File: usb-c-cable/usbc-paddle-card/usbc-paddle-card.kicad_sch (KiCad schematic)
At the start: 7 parts, among them J1 USB_C_Receptacle, P1 PAD_SMD, P2 PAD_SMD, P3 PAD_SMD, P4 PAD_SMD, P5 PAD_SMD

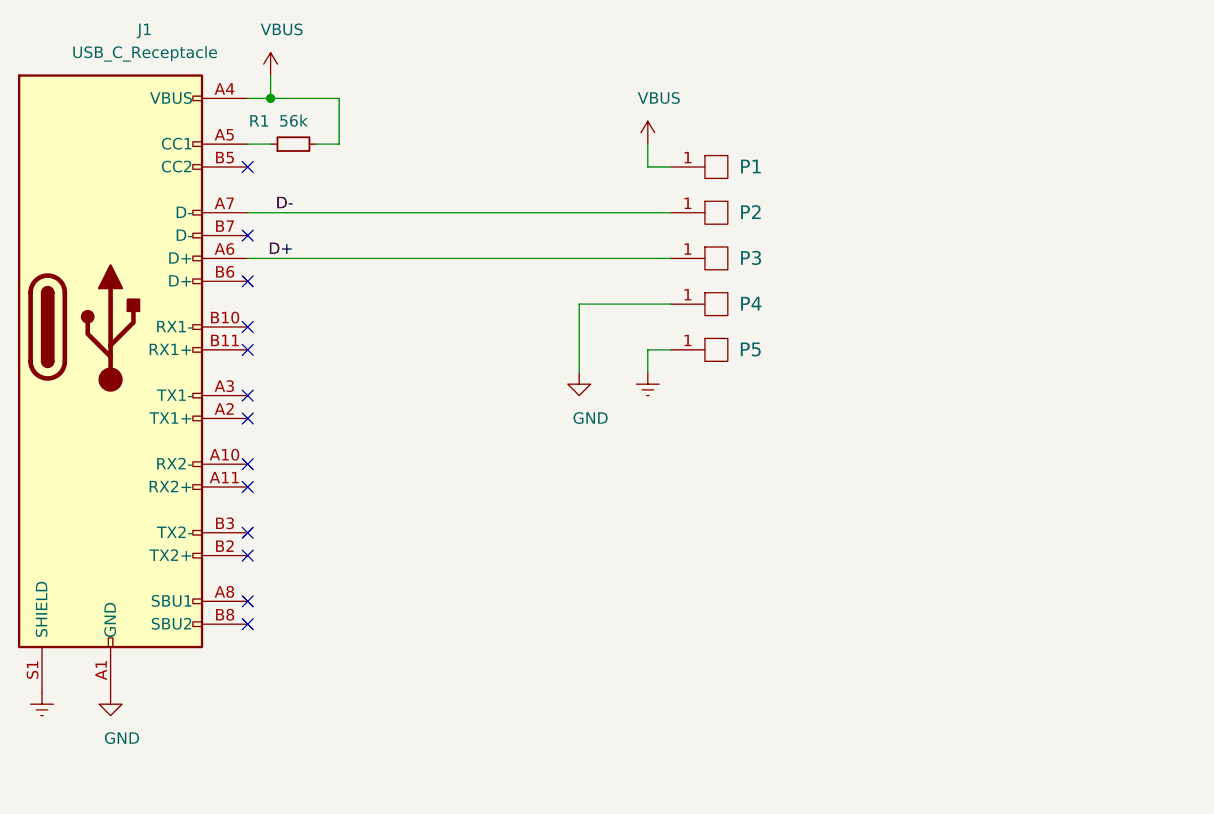
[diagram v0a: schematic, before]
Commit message: Added resistor value for up-stream facing paddle use.
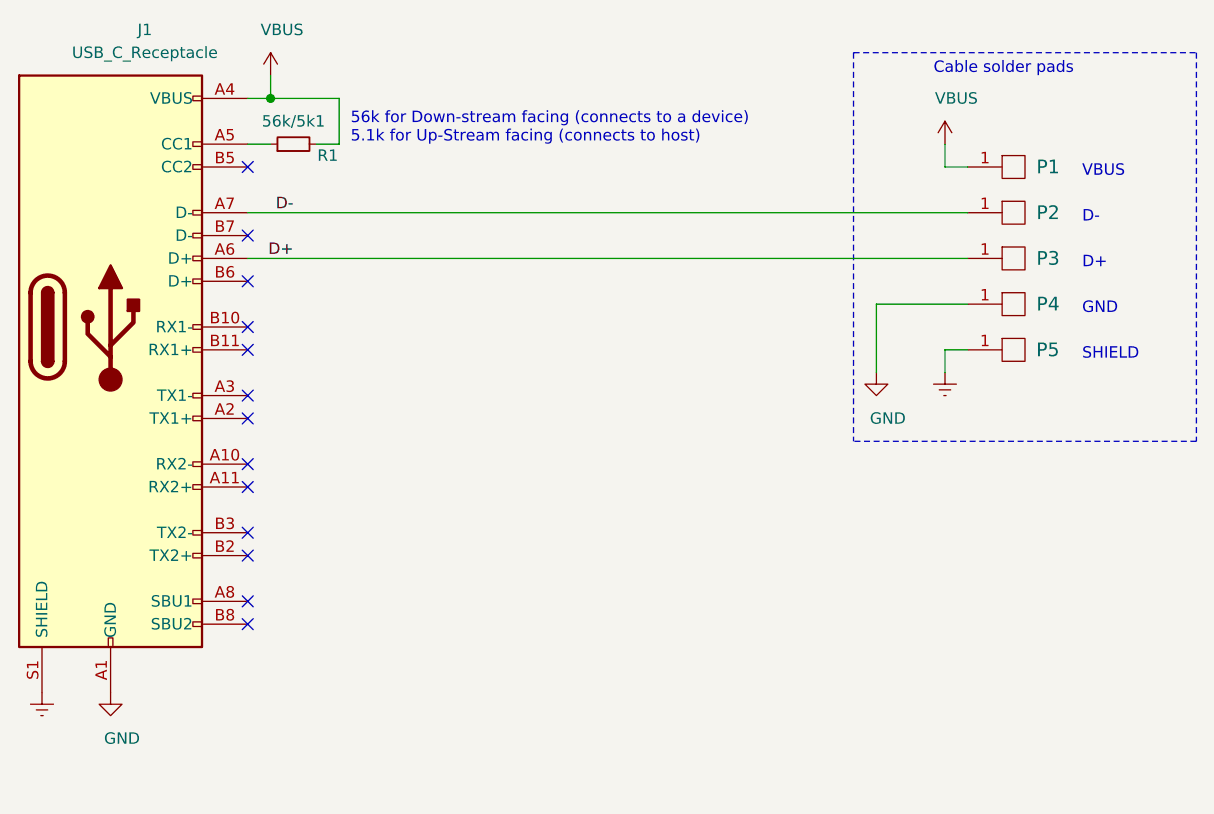
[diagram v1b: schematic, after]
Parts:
- R1: value 56k -> 56k/5k1
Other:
- note added: "56k for Down-stream facing (connects to a device) 5.1k for Up-Stream facing (connects to host)"
- note added: "Cable solder pads"
- note added: "D+"
- note added: "D-"
- note added: "GND"
- note added: "SHIELD"
- note added: "VBUS"
- moved on the sheet: P1, P2, P3, P4, P5

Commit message: Added resistor for Up-Stream use.
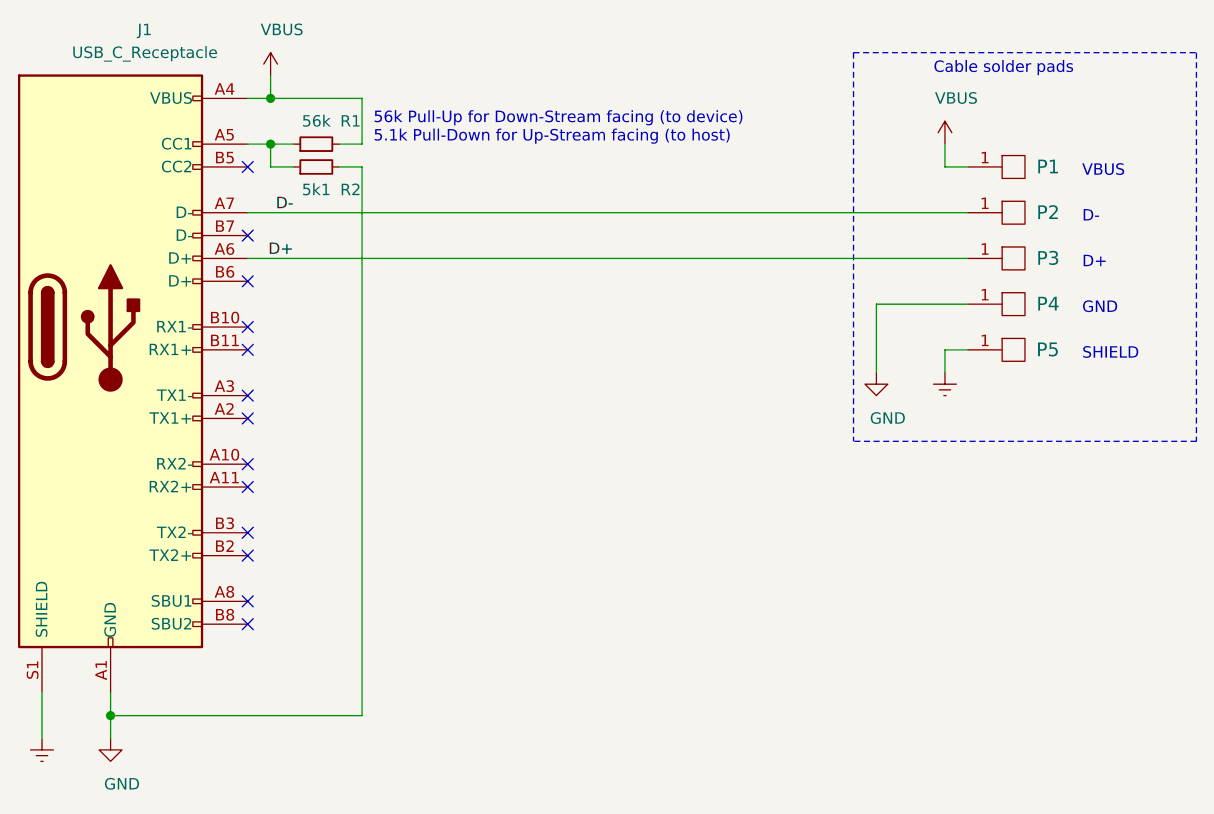
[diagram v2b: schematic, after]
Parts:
- added R2: 5k1, pkl_dipol:R_0402, symbol pkl_device:pkl_R_Small
- R1: value 56k/5k1 -> 56k
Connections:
- net GND: now also R2.2
- net at J1.A5 (CC1), R1.1: now also R2.1
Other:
- note added: "56k Pull-Up for Down-Stream facing (to device) 5.1k Pull-Down for Up-Stream facing (to host)"
- note removed: "56k for Down-stream facing (connects to a device) 5.1k for Up-Stream facing (connects to host)"
- moved on the sheet: R1
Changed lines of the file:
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@@
   (page 1 1)
   (paper "A4")
+  (junction (at 36.83 107.95) (diameter 1.016) (color 0 0 0 0))
   (junction (at 54.61 39.37) (diameter 1.016) (color 0 0 0 0))
+  (junction (at 54.61 44.45) (diameter 1.016) (color 0 0 0 0))
+  (no_connect (at 52.07 74.93))
+  (no_connect (at 52.07 90.17))
+  (no_connect (at 52.07 46.99))
+  (no_connect (at 52.07 95.25))
+  (no_connect (at 52.07 80.01))
+  (no_connect (at 52.07 54.61))
+  (no_connect (at 52.07 59.69))
   (no_connect (at 52.07 64.77))
+  (no_connect (at 52.07 72.39))
   (no_connect (at 52.07 67.31))
-  (no_connect (at 52.07 46.99))
   (no_connect (at 52.07 97.79))
-  (no_connect (at 52.07 72.39))
-  (no_connect (at 52.07 95.25))
-  (no_connect (at 52.07 90.17))
-  (no_connect (at 52.07 54.61))
+  (no_connect (at 52.07 82.55))
   (no_connect (at 52.07 87.63))
-  (no_connect (at 52.07 74.93))
-  (no_connect (at 52.07 80.01))
-  (no_connect (at 52.07 59.69))
-  (no_connect (at 52.07 82.55))
+  (wire (pts (xy 29.21 110.49) (xy 29.21 105.41))
+    (stroke (width 0) (type solid) (color 0 0 0 0))
+  )
+  (wire (pts (xy 36.83 107.95) (xy 36.83 105.41))
+    (stroke (width 0) (type solid) (color 0 0 0 0))
+  )
+  (wire (pts (xy 36.83 107.95) (xy 64.77 107.95))
+    (stroke (width 0) (type solid) (color 0 0 0 0))
+  )
+  (wire (pts (xy 36.83 110.49) (xy 36.83 107.95))
+    (stroke (width 0) (type solid) (color 0 0 0 0))
+  )
   (wire (pts (xy 52.07 39.37) (xy 54.61 39.37))
     (stroke (width 0) (type solid) (color 0 0 0 0))
@@
     (stroke (width 0) (type solid) (color 0 0 0 0))
   )
-  (wire (pts (xy 54.61 39.37) (xy 62.23 39.37))
-    (stroke (width 0) (type solid) (color 0 0 0 0))
-  )
-  (wire (pts (xy 59.69 44.45) (xy 62.23 44.45))
-    (stroke (width 0) (type solid) (color 0 0 0 0))
-  )
-  (wire (pts (xy 62.23 44.45) (xy 62.23 39.37))
+  (wire (pts (xy 54.61 39.37) (xy 64.77 39.37))
+    (stroke (width 0) (type solid) (color 0 0 0 0))
+  )
+  (wire (pts (xy 54.61 44.45) (xy 57.15 44.45))
+    (stroke (width 0) (type solid) (color 0 0 0 0))
+  )
+  (wire (pts (xy 54.61 46.99) (xy 54.61 44.45))
+    (stroke (width 0) (type solid) (color 0 0 0 0))
+  )
+  (wire (pts (xy 57.15 46.99) (xy 54.61 46.99))
+    (stroke (width 0) (type solid) (color 0 0 0 0))
+  )
+  (wire (pts (xy 62.23 44.45) (xy 64.77 44.45))
+    (stroke (width 0) (type solid) (color 0 0 0 0))
+  )
+  (wire (pts (xy 64.77 44.45) (xy 64.77 39.37))
+    (stroke (width 0) (type solid) (color 0 0 0 0))
+  )
+  (wire (pts (xy 64.77 46.99) (xy 62.23 46.99))
+    (stroke (width 0) (type solid) (color 0 0 0 0))
+  )
+  (wire (pts (xy 64.77 107.95) (xy 64.77 46.99))
     (stroke (width 0) (type solid) (color 0 0 0 0))
   )
@@
     (stroke (width 0) (type dash) (color 0 0 0 0))
   )
-  (text "56k for Down-stream facing (connects to a device)\n5.1k for Up-Stream facing (connects to host)"
-    (at 63.5 44.45 0)
+  (text "56k Pull-Up for Down-Stream facing (to device)\n5.1k Pull-Down for Up-Stream facing (to host)"
+    (at 66.04 44.45 0)
     (effects (font (size 1.27 1.27)) (justify left bottom))
   )
@@
     )
   )
-  (symbol (lib_id "power:Earth") (at 29.21 105.41 0) (unit 1)
-    (in_bom yes) (on_board yes)
-    (property "Reference" "#PWR0101" (id 0) (at 29.21 111.76 0)
-      (effects (font (size 1.27 1.27)) hide)
-    )
-    (property "Value" "Earth" (id 1) (at 29.21 109.22 0)
-      (effects (font (size 1.27 1.27)) hide)
-    )
-    (property "Footprint" "" (id 2) (at 29.21 105.41 0)
-      (effects (font (size 1.27 1.27)) hide)
-    )
-    (property "Datasheet" "~" (id 3) (at 29.21 105.41 0)
-      (effects (font (size 1.27 1.27)) hide)
-    )
-  )
-  (symbol (lib_id "power:GND") (at 36.83 105.41 0) (unit 1)
-    (in_bom yes) (on_board yes)
-    (property "Reference" "#PWR0102" (id 0) (at 36.83 111.76 0)
-      (effects (font (size 1.27 1.27)) hide)
-    )
-    (property "Value" "GND" (id 1) (at 38.1 110.49 0))
-    (property "Footprint" "" (id 2) (at 36.83 105.41 0)
-      (effects (font (size 1.27 1.27)) hide)
-    )
-    (property "Datasheet" "" (id 3) (at 36.83 105.41 0)
+  (symbol (lib_id "power:Earth") (at 29.21 110.49 0) (unit 1)
+    (in_bom yes) (on_board yes)
+    (property "Reference" "#PWR0101" (id 0) (at 29.21 116.84 0)
+      (effects (font (size 1.27 1.27)) hide)
+    )
+    (property "Value" "Earth" (id 1) (at 29.21 114.3 0)
+      (effects (font (size 1.27 1.27)) hide)
+    )
+    (property "Footprint" "" (id 2) (at 29.21 110.49 0)
+      (effects (font (size 1.27 1.27)) hide)
+    )
+    (property "Datasheet" "~" (id 3) (at 29.21 110.49 0)
+      (effects (font (size 1.27 1.27)) hide)
+    )
+  )
+  (symbol (lib_id "power:GND") (at 36.83 110.49 0) (unit 1)
+    (in_bom yes) (on_board yes)
+    (property "Reference" "#PWR0102" (id 0) (at 36.83 116.84 0)
+      (effects (font (size 1.27 1.27)) hide)
+    )
+    (property "Value" "GND" (id 1) (at 38.1 115.57 0))
+    (property "Footprint" "" (id 2) (at 36.83 110.49 0)
+      (effects (font (size 1.27 1.27)) hide)
+    )
+    (property "Datasheet" "" (id 3) (at 36.83 110.49 0)
       (effects (font (size 1.27 1.27)) hide)
     )
@@
     )
   )
-  (symbol (lib_id "pkl_device:pkl_R_Small") (at 57.15 44.45 90) (unit 1)
-    (in_bom yes) (on_board yes)
-    (property "Reference" "R1" (id 0) (at 60.96 45.72 90))
-    (property "Value" "56k/5k1" (id 1) (at 57.15 41.91 90))
-    (property "Footprint" "pkl_dipol:R_0402" (id 2) (at 57.15 44.45 0)
-      (effects (font (size 1.524 1.524)) hide)
-    )
-    (property "Datasheet" "" (id 3) (at 57.15 44.45 0)
+  (symbol (lib_id "pkl_device:pkl_R_Small") (at 59.69 44.45 90) (unit 1)
+    (in_bom yes) (on_board yes)
+    (property "Reference" "R1" (id 0) (at 63.5 41.91 90))
+    (property "Value" "56k" (id 1) (at 59.69 41.91 90))
+    (property "Footprint" "pkl_dipol:R_0402" (id 2) (at 59.69 44.45 0)
+      (effects (font (size 1.524 1.524)) hide)
+    )
+    (property "Datasheet" "" (id 3) (at 59.69 44.45 0)
+      (effects (font (size 1.524 1.524)))
+    )
+  )
+  (symbol (lib_id "pkl_device:pkl_R_Small") (at 59.69 46.99 90) (unit 1)
+    (in_bom yes) (on_board yes)
+    (property "Reference" "R2" (id 0) (at 63.5 49.53 90))
+    (property "Value" "5k1" (id 1) (at 59.69 49.53 90))
+    (property "Footprint" "pkl_dipol:R_0402" (id 2) (at 59.69 46.99 0)
+      (effects (font (size 1.524 1.524)) hide)
+    )
+    (property "Datasheet" "" (id 3) (at 59.69 46.99 0)
       (effects (font (size 1.524 1.524)))
     )
@@
     )
     (path "/16905efd-176f-45e2-8af2-45df7d4754db"
-      (reference "R1") (unit 1) (value "56k/5k1") (footprint "pkl_dipol:R_0402")
-    )
-  )
+      (reference "R1") (unit 1) (value "56k") (footprint "pkl_dipol:R_0402")
+    )
+    (path "/be23b02b-e33a-45da-bd4e-4d5cbc312d42"
+      (reference "R2") (unit 1) (value "5k1") (footprint "pkl_dipol:R_0402")
+    )
+  )
